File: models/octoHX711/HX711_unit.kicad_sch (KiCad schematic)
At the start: 12 parts

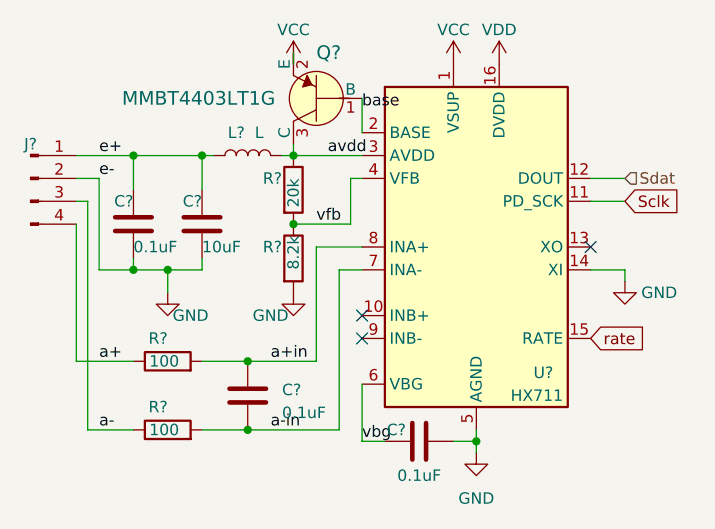
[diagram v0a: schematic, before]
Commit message: fixed silkscreen and added arduino lib
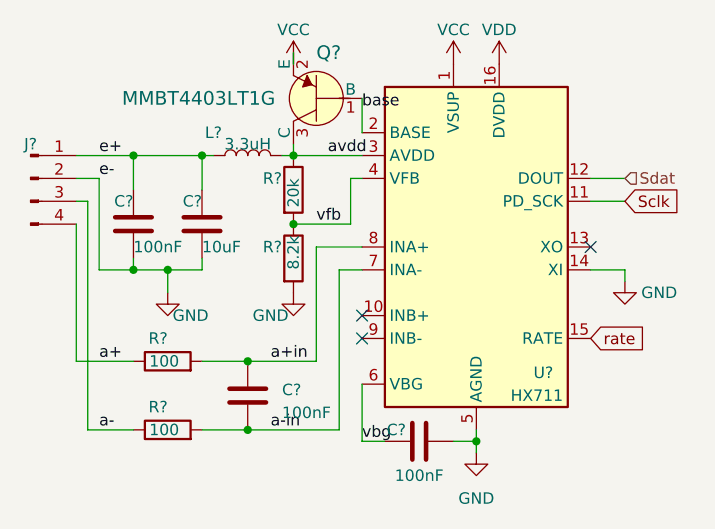
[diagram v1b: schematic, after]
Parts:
- C? (x3): value 0.1uF -> 100nF
- L?: value L -> 3.3uH
- R? (x4): footprint Resistor_SMD:R_01005_0402Metric -> Resistor_SMD:R_0402_1005Metric
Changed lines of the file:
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@@
       (effects (font (size 1.27 1.27)) (justify right))
     )
-    (property "Footprint" "Resistor_SMD:R_01005_0402Metric" (at 143.002 85.09 90)
+    (property "Footprint" "Resistor_SMD:R_0402_1005Metric" (at 143.002 85.09 90)
       (effects (font (size 1.27 1.27)) hide)
     )
@@
       (effects (font (size 1.27 1.27)) (justify left))
     )
-    (property "Footprint" "Resistor_SMD:R_01005_0402Metric" (at 130.81 98.298 90)
+    (property "Footprint" "Resistor_SMD:R_0402_1005Metric" (at 130.81 98.298 90)
       (effects (font (size 1.27 1.27)) hide)
     )
@@
       (effects (font (size 1.27 1.27)) (justify left))
     )
-    (property "Footprint" "Resistor_SMD:R_01005_0402Metric" (at 130.81 105.918 90)
+    (property "Footprint" "Resistor_SMD:R_0402_1005Metric" (at 130.81 105.918 90)
       (effects (font (size 1.27 1.27)) hide)
     )
@@
       (effects (font (size 1.27 1.27)) (justify right))
     )
-    (property "Footprint" "Resistor_SMD:R_01005_0402Metric" (at 143.002 77.47 90)
+    (property "Footprint" "Resistor_SMD:R_0402_1005Metric" (at 143.002 77.47 90)
       (effects (font (size 1.27 1.27)) hide)
     )
@@
   (symbol (lib_id "Device:L") (at 139.7 73.66 90) (unit 1)
     (in_bom yes) (on_board yes) (dnp no)
-    (property "Reference" "L?" (at 138.43 71.12 90)
-      (effects (font (size 1.27 1.27)))
-    )
-    (property "Value" "L" (at 140.97 71.12 90)
+    (property "Reference" "L?" (at 135.89 71.12 90)
+      (effects (font (size 1.27 1.27)))
+    )
+    (property "Value" "3.3uH" (at 139.7 72.39 90)
       (effects (font (size 1.27 1.27)))
     )
@@
       (effects (font (size 1.27 1.27)) (justify left))
     )
-    (property "Value" "0.1uF" (at 143.51 102.235 0)
+    (property "Value" "100nF" (at 143.51 102.235 0)
       (effects (font (size 1.27 1.27)) (justify left))
     )
@@
       (effects (font (size 1.27 1.27)) (justify right))
     )
-    (property "Value" "0.1uF" (at 127 83.82 0)
+    (property "Value" "100nF" (at 127 83.82 0)
       (effects (font (size 1.27 1.27)) (justify left))
     )
@@
       (effects (font (size 1.27 1.27)))
     )
-    (property "Value" "0.1uF" (at 158.75 109.22 90)
-      (effects (font (size 1.27 1.27)))
-    )
+    (property "Value" "100nF" (at 158.75 109.22 90)
+      (effects (font (size 1.27 1.27)))
+    )
